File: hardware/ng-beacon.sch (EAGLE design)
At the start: 7 parts

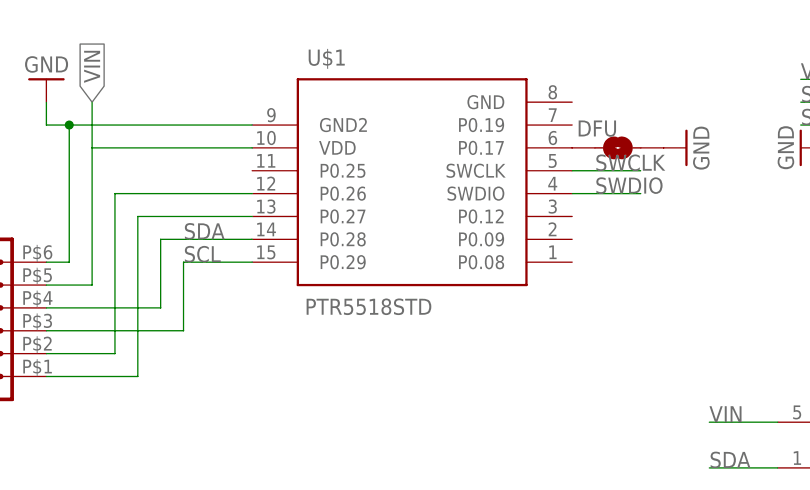
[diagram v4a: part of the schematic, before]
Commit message: Convert to PTR5618, export components to project-specific library.
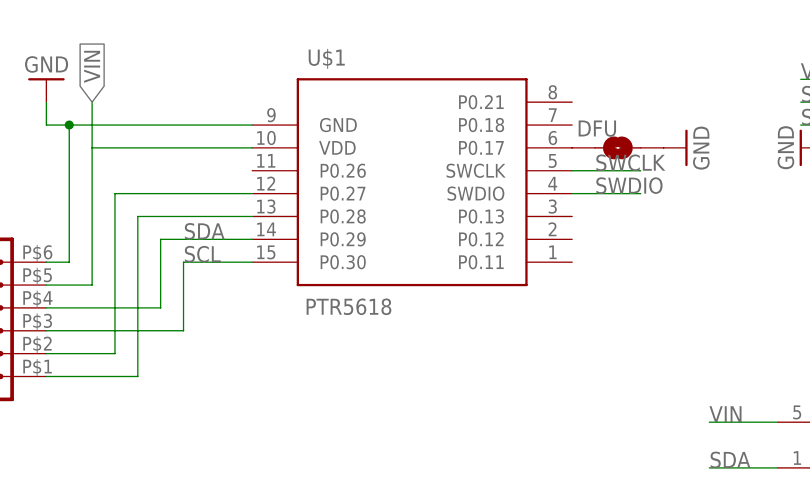
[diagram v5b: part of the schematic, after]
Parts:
- G1: device SparkFun-Electromechanical:BATTERY20MM_4LEGS -> ng-beacon:BATTERY20MM_4LEGS
- J3: device heathkit:CONN_06 -> ng-beacon:CONN_06
- S1: device SparkFun-Electromechanical:SWITCH-DPDTAYZ0202 -> ng-beacon:SWITCH-DPDTAYZ0202
- SN1: device sensirion:SHT21 -> ng-beacon:SHT21
- U$1: value PTR5518STD -> PTR5618; device PTR5518:PTR5518STD -> ng-beacon:PTR5618
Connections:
- net GND: now also U$1.GND; no longer U$1.GND2
- net N$5: now also U$1.P0.27; no longer U$1.P0.26
- net N$6: now also U$1.P0.28; no longer U$1.P0.27
- net SCL: now also U$1.P0.30; no longer U$1.P0.29
- net SDA: now also U$1.P0.29; no longer U$1.P0.28
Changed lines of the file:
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@@
 </classes>
 <parts>
-<part name="U$1" library="PTR5518" deviceset="PTR5518" device="STD"/>
-<part name="G1" library="SparkFun-Electromechanical" deviceset="BATTERY" device="20MM_4LEGS" value="20mm coincell"/>
-<part name="S1" library="SparkFun-Electromechanical" deviceset="SWITCH-DPDT" device="AYZ0202" value="DPDT"/>
+<part name="U$1" library="ng-beacon" deviceset="PTR5618" device=""/>
+<part name="G1" library="ng-beacon" deviceset="BATTERY" device="20MM_4LEGS" value="20mm coincell"/>
+<part name="S1" library="ng-beacon" deviceset="SWITCH-DPDT" device="AYZ0202" value="DPDT"/>
 <part name="GND1" library="SparkFun-Aesthetics" deviceset="GND" device=""/>
 <part name="GND3" library="SparkFun-Aesthetics" deviceset="GND" device=""/>
 <part name="J1" library="SparkFun-Connectors" deviceset="M04" device="LOCK"/>
 <part name="GND8" library="SparkFun-Aesthetics" deviceset="GND" device=""/>
-<part name="SN1" library="sensirion" deviceset="SHT21" device=""/>
+<part name="SN1" library="ng-beacon" deviceset="SHT21" device=""/>
 <part name="GND4" library="SparkFun-Aesthetics" deviceset="GND" device=""/>
 <part name="DFU" library="SparkFun-Passives" deviceset="JUMPER-PAD-2-NO" device=""/>
 <part name="GND5" library="SparkFun-Aesthetics" deviceset="GND" device=""/>
-<part name="J3" library="heathkit" deviceset="CONN_06" device=""/>
+<part name="J3" library="ng-beacon" deviceset="CONN_06" device=""/>
 </parts>
 <sheets>
@@
 </segment>
 <segment>
-<pinref part="U$1" gate="G$1" pin="GND2"/>
+<pinref part="U$1" gate="G$1" pin="GND"/>
 <wire x1="12.7" y1="81.28" x2="12.7" y2="78.74" width="0.1524" layer="91"/>
 <wire x1="12.7" y1="78.74" x2="15.24" y2="78.74" width="0.1524" layer="91"/>
@@
 <net name="SDA" class="0">
 <segment>
-<pinref part="U$1" gate="G$1" pin="P0.28"/>
+<pinref part="U$1" gate="G$1" pin="P0.29"/>
 <label x="27.94" y="66.04" size="1.778" layer="95"/>
 <wire x1="35.56" y1="66.04" x2="25.4" y2="66.04" width="0.1524" layer="91"/>
@@
 <net name="SCL" class="0">
 <segment>
-<pinref part="U$1" gate="G$1" pin="P0.29"/>
+<pinref part="U$1" gate="G$1" pin="P0.30"/>
 <label x="27.94" y="63.5" size="1.778" layer="95"/>
 <wire x1="35.56" y1="63.5" x2="27.94" y2="63.5" width="0.1524" layer="91"/>
@@
 <segment>
 <wire x1="20.32" y1="53.34" x2="20.32" y2="71.12" width="0.1524" layer="91"/>
-<pinref part="U$1" gate="G$1" pin="P0.26"/>
+<pinref part="U$1" gate="G$1" pin="P0.27"/>
 <wire x1="20.32" y1="71.12" x2="35.56" y2="71.12" width="0.1524" layer="91"/>
 <pinref part="J3" gate="G$1" pin="2"/>
@@
 <segment>
 <wire x1="22.86" y1="50.8" x2="22.86" y2="68.58" width="0.1524" layer="91"/>
-<pinref part="U$1" gate="G$1" pin="P0.27"/>
+<pinref part="U$1" gate="G$1" pin="P0.28"/>
 <wire x1="22.86" y1="68.58" x2="35.56" y2="68.58" width="0.1524" layer="91"/>
 <pinref part="J3" gate="G$1" pin="1"/>

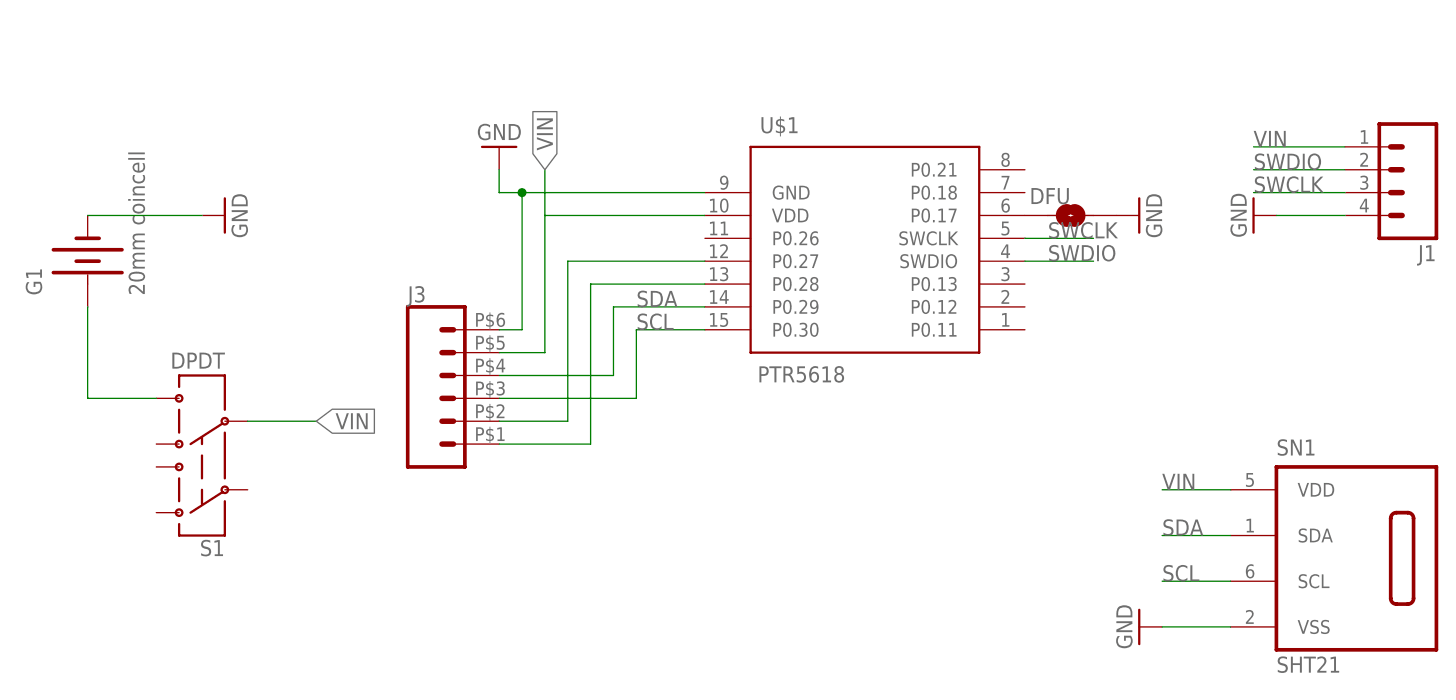
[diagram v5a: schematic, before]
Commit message: move the proto version of a different file
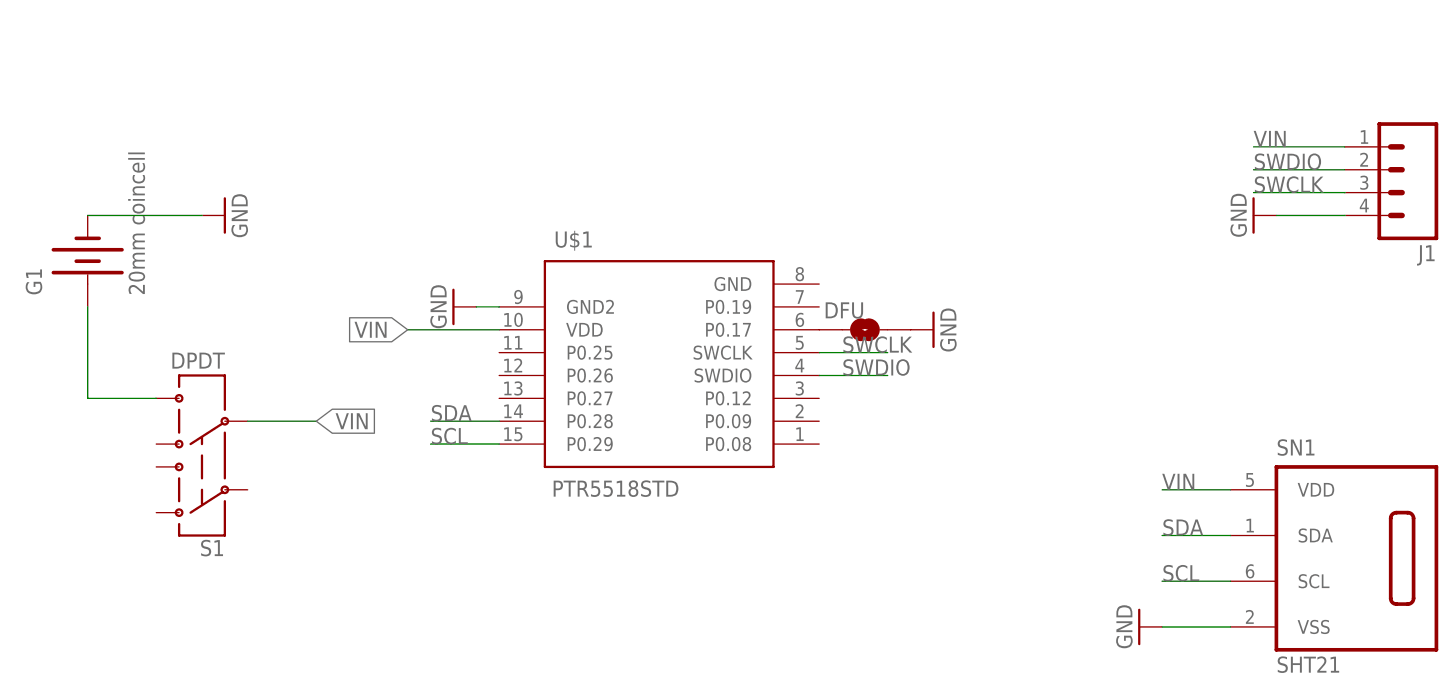
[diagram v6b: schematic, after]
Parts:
- removed J3: (no value), ng-beacon:CONN_06
- G1: device ng-beacon:BATTERY20MM_4LEGS -> SparkFun-Electromechanical:BATTERY20MM_4LEGS
- S1: device ng-beacon:SWITCH-DPDTAYZ0202 -> SparkFun-Electromechanical:SWITCH-DPDTAYZ0202
- SN1: device ng-beacon:SHT21 -> sensirion:SHT21
- U$1: value PTR5618 -> PTR5518STD; device ng-beacon:PTR5618 -> PTR5518:PTR5518STD
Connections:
- removed net N$5: J3.2, U$1.P0.27
- removed net N$6: J3.1, U$1.P0.28
- net GND: now also U$1.GND2; no longer J3.6, U$1.GND
- net SCL: now also U$1.P0.29; no longer J3.3, U$1.P0.30
- net SDA: now also U$1.P0.28; no longer J3.4, U$1.P0.29
- net VIN: no longer J3.5
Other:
- moved on the sheet: DFU, U$1
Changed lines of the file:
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@@
 <?xml version="1.0" encoding="utf-8"?>
 <!DOCTYPE eagle SYSTEM "eagle.dtd">
-<eagle version="8.0.2">
+<eagle version="7.6.0">
 <drawing>
 <settings>
@@
 </classes>
 <parts>
-<part name="U$1" library="ng-beacon" deviceset="PTR5618" device=""/>
-<part name="G1" library="ng-beacon" deviceset="BATTERY" device="20MM_4LEGS" value="20mm coincell"/>
-<part name="S1" library="ng-beacon" deviceset="SWITCH-DPDT" device="AYZ0202" value="DPDT"/>
+<part name="U$1" library="PTR5518" deviceset="PTR5518" device="STD"/>
+<part name="G1" library="SparkFun-Electromechanical" deviceset="BATTERY" device="20MM_4LEGS" value="20mm coincell"/>
+<part name="S1" library="SparkFun-Electromechanical" deviceset="SWITCH-DPDT" device="AYZ0202" value="DPDT"/>
 <part name="GND1" library="SparkFun-Aesthetics" deviceset="GND" device=""/>
 <part name="GND3" library="SparkFun-Aesthetics" deviceset="GND" device=""/>
 <part name="J1" library="SparkFun-Connectors" deviceset="M04" device="LOCK"/>
 <part name="GND8" library="SparkFun-Aesthetics" deviceset="GND" device=""/>
-<part name="SN1" library="ng-beacon" deviceset="SHT21" device=""/>
+<part name="SN1" library="sensirion" deviceset="SHT21" device=""/>
 <part name="GND4" library="SparkFun-Aesthetics" deviceset="GND" device=""/>
 <part name="DFU" library="SparkFun-Passives" deviceset="JUMPER-PAD-2-NO" device=""/>
 <part name="GND5" library="SparkFun-Aesthetics" deviceset="GND" device=""/>
-<part name="J3" library="ng-beacon" deviceset="CONN_06" device=""/>
 </parts>
 <sheets>
@@
 </plain>
 <instances>
-<instance part="U$1" gate="G$1" x="53.34" y="71.12"/>
+<instance part="U$1" gate="G$1" x="30.48" y="58.42"/>
 <instance part="G1" gate="G$1" x="-33.02" y="71.12" rot="R90"/>
 <instance part="S1" gate="G$1" x="-20.32" y="48.26" rot="R180"/>
 <instance part="GND1" gate="1" x="-17.78" y="76.2" rot="R90"/>
-<instance part="GND3" gate="1" x="12.7" y="83.82" rot="R180"/>
+<instance part="GND3" gate="1" x="7.62" y="66.04" rot="R270"/>
 <instance part="J1" gate="G$1" x="111.76" y="81.28" rot="R180"/>
 <instance part="GND8" gate="1" x="96.52" y="76.2" rot="R270"/>
 <instance part="SN1" gate="G$1" x="106.68" y="38.1"/>
 <instance part="GND4" gate="1" x="83.82" y="30.48" rot="R270"/>
-<instance part="DFU" gate="G$1" x="76.2" y="76.2" smashed="yes">
-<attribute name="NAME" x="71.628" y="77.47" size="1.778" layer="95"/>
+<instance part="DFU" gate="G$1" x="53.34" y="63.5" smashed="yes">
+<attribute name="NAME" x="48.768" y="64.77" size="1.778" layer="95"/>
 </instance>
-<instance part="GND5" gate="1" x="83.82" y="76.2" rot="R90"/>
-<instance part="J3" gate="G$1" x="7.62" y="55.88"/>
+<instance part="GND5" gate="1" x="60.96" y="63.5" rot="R90"/>
 </instances>
 <busses>
@@
 </segment>
 <segment>
-<pinref part="U$1" gate="G$1" pin="GND"/>
-<wire x1="12.7" y1="81.28" x2="12.7" y2="78.74" width="0.1524" layer="91"/>
-<wire x1="12.7" y1="78.74" x2="15.24" y2="78.74" width="0.1524" layer="91"/>
+<pinref part="U$1" gate="G$1" pin="GND2"/>
+<wire x1="10.16" y1="66.04" x2="12.7" y2="66.04" width="0.1524" layer="91"/>
 <pinref part="GND3" gate="1" pin="GND"/>
-<pinref part="J3" gate="G$1" pin="6"/>
-<wire x1="15.24" y1="78.74" x2="35.56" y2="78.74" width="0.1524" layer="91"/>
-<wire x1="12.7" y1="63.5" x2="15.24" y2="63.5" width="0.1524" layer="91"/>
-<wire x1="15.24" y1="63.5" x2="15.24" y2="78.74" width="0.1524" layer="91"/>
-<junction x="15.24" y="78.74"/>
 </segment>
 <segment>
@@
 <segment>
 <pinref part="U$1" gate="G$1" pin="VDD"/>
-<wire x1="35.56" y1="76.2" x2="17.78" y2="76.2" width="0.1524" layer="91"/>
-<wire x1="17.78" y1="76.2" x2="17.78" y2="81.28" width="0.1524" layer="91"/>
-<label x="17.78" y="81.28" size="1.778" layer="95" rot="R90" xref="yes"/>
-<wire x1="17.78" y1="76.2" x2="17.78" y2="60.96" width="0.1524" layer="91"/>
-<pinref part="J3" gate="G$1" pin="5"/>
-<wire x1="12.7" y1="60.96" x2="17.78" y2="60.96" width="0.1524" layer="91"/>
+<wire x1="12.7" y1="63.5" x2="2.54" y2="63.5" width="0.1524" layer="91"/>
+<label x="2.54" y="63.5" size="1.778" layer="95" rot="R180" xref="yes"/>
 </segment>
 <segment>
@@
 <segment>
 <pinref part="U$1" gate="G$1" pin="SWCLK"/>
-<wire x1="71.12" y1="73.66" x2="78.74" y2="73.66" width="0.1524" layer="91"/>
-<label x="73.66" y="73.66" size="1.778" layer="95"/>
+<wire x1="48.26" y1="60.96" x2="55.88" y2="60.96" width="0.1524" layer="91"/>
+<label x="50.8" y="60.96" size="1.778" layer="95"/>
 </segment>
 </net>
@@
 <segment>
 <pinref part="U$1" gate="G$1" pin="SWDIO"/>
-<wire x1="71.12" y1="71.12" x2="78.74" y2="71.12" width="0.1524" layer="91"/>
-<label x="73.66" y="71.12" size="1.778" layer="95"/>
+<wire x1="48.26" y1="58.42" x2="55.88" y2="58.42" width="0.1524" layer="91"/>
+<label x="50.8" y="58.42" size="1.778" layer="95"/>
 </segment>
 </net>
 <net name="SDA" class="0">
 <segment>
-<pinref part="U$1" gate="G$1" pin="P0.29"/>
-<label x="27.94" y="66.04" size="1.778" layer="95"/>
-<wire x1="35.56" y1="66.04" x2="25.4" y2="66.04" width="0.1524" layer="91"/>
-<pinref part="J3" gate="G$1" pin="4"/>
-<wire x1="12.7" y1="58.42" x2="25.4" y2="58.42" width="0.1524" layer="91"/>
-<wire x1="25.4" y1="58.42" x2="25.4" y2="66.04" width="0.1524" layer="91"/>
+<pinref part="U$1" gate="G$1" pin="P0.28"/>
+<wire x1="12.7" y1="53.34" x2="5.08" y2="53.34" width="0.1524" layer="91"/>
+<label x="5.08" y="53.34" size="1.778" layer="95"/>
 </segment>
 <segment>
@@
 <net name="SCL" class="0">
 <segment>
-<pinref part="U$1" gate="G$1" pin="P0.30"/>
-<label x="27.94" y="63.5" size="1.778" layer="95"/>
-<wire x1="35.56" y1="63.5" x2="27.94" y2="63.5" width="0.1524" layer="91"/>
-<pinref part="J3" gate="G$1" pin="3"/>
-<wire x1="12.7" y1="55.88" x2="27.94" y2="55.88" width="0.1524" layer="91"/>
-<wire x1="27.94" y1="55.88" x2="27.94" y2="63.5" width="0.1524" layer="91"/>
+<pinref part="U$1" gate="G$1" pin="P0.29"/>
+<wire x1="12.7" y1="50.8" x2="5.08" y2="50.8" width="0.1524" layer="91"/>
+<label x="5.08" y="50.8" size="1.778" layer="95"/>
 </segment>
 <segment>
@@
 </segment>
 </net>
-<net name="N$5" class="0">
-<segment>
-<wire x1="20.32" y1="53.34" x2="20.32" y2="71.12" width="0.1524" layer="91"/>
-<pinref part="U$1" gate="G$1" pin="P0.27"/>
-<wire x1="20.32" y1="71.12" x2="35.56" y2="71.12" width="0.1524" layer="91"/>
-<pinref part="J3" gate="G$1" pin="2"/>
-<wire x1="12.7" y1="53.34" x2="20.32" y2="53.34" width="0.1524" layer="91"/>
-</segment>
-</net>
-<net name="N$6" class="0">
-<segment>
-<wire x1="22.86" y1="50.8" x2="22.86" y2="68.58" width="0.1524" layer="91"/>
-<pinref part="U$1" gate="G$1" pin="P0.28"/>
-<wire x1="22.86" y1="68.58" x2="35.56" y2="68.58" width="0.1524" layer="91"/>
-<pinref part="J3" gate="G$1" pin="1"/>
-<wire x1="12.7" y1="50.8" x2="22.86" y2="50.8" width="0.1524" layer="91"/>
-</segment>
-</net>
